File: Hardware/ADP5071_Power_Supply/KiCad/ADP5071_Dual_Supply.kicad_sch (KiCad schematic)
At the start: 42 parts, among them J1 MountingPin, J2 Screw_Terminal_01x02, J3 Conn_01x03_Pin, J4 MountingPin, J5 MountingPin, J6 MountingPin, U1 ADP5071AREZ

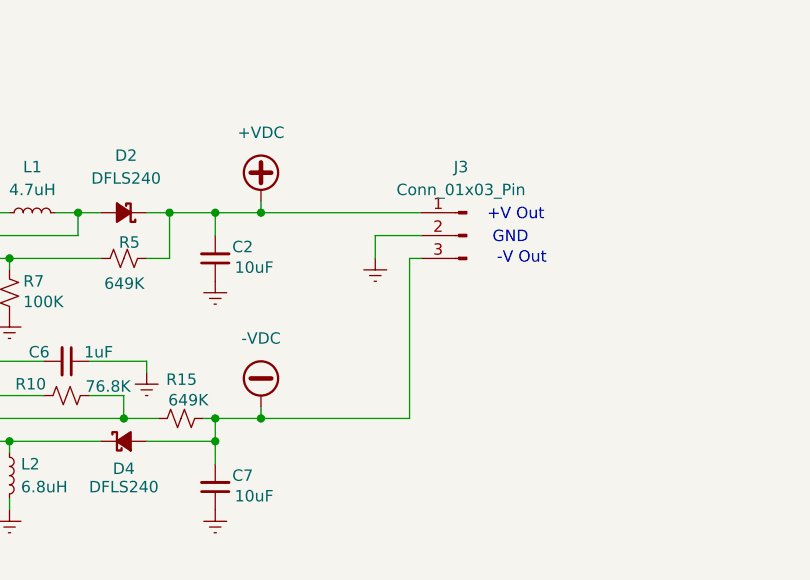
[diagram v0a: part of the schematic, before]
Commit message: added connector for dual board power delivery
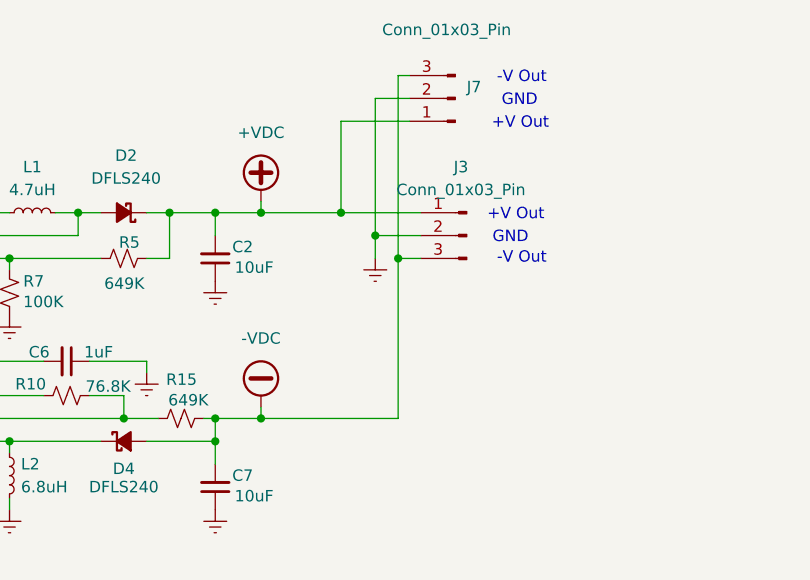
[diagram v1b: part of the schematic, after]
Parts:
- added J7: Conn_01x03_Pin, Connector_PinHeader_2.54mm:PinHeader_1x03_P2.54mm_Horizontal, symbol Connector:Conn_01x03_Pin
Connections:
- net +VDC: now also J7.1 (Pin_1)
- net -VDC: now also J7.3 (Pin_3)
- net GNDREF: now also J7.2 (Pin_2)
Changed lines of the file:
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@@
 		)
 	)
+	(text "-V Out"
+		(exclude_from_sim no)
+		(at 222.25 65.786 0)
+		(effects
+			(font
+				(size 1.27 1.27)
+			)
+			(justify right bottom)
+		)
+	)
 	(text "+V Out"
 		(exclude_from_sim no)
@@
 		)
 	)
+	(text "GND"
+		(exclude_from_sim no)
+		(at 221.234 68.326 0)
+		(effects
+			(font
+				(size 1.27 1.27)
+			)
+			(justify right bottom)
+		)
+	)
+	(text "+V Out"
+		(exclude_from_sim no)
+		(at 222.504 70.866 0)
+		(effects
+			(font
+				(size 1.27 1.27)
+			)
+			(justify right bottom)
+		)
+	)
 	(junction
 		(at 160.02 100.33)
@@
 	)
 	(junction
+		(at 205.74 85.09)
+		(diameter 0)
+		(color 0 0 0 0)
+	)
+	(junction
 		(at 99.06 90.17)
 		(diameter 0)
@@
 	)
 	(junction
+		(at 203.2 82.55)
+		(diameter 0)
+		(color 0 0 0 0)
+	)
+	(junction
 		(at 105.41 133.35)
 		(diameter 0)
@@
 	)
 	(junction
+		(at 199.39 80.01)
+		(diameter 0)
+		(color 0 0 0 0)
+	)
+	(junction
 		(at 127 85.09)
 		(diameter 0)
@@
 	(wire
 		(pts
+			(xy 205.74 85.09) (xy 208.28 85.09)
+		)
+		(stroke
+			(width 0)
+			(type default)
+		)
+	)
+	(wire
+		(pts
 			(xy 80.01 76.2) (xy 80.01 85.09)
 		)
@@
 	(wire
 		(pts
-			(xy 190.5 80.01) (xy 208.28 80.01)
+			(xy 190.5 80.01) (xy 199.39 80.01)
 		)
 		(stroke
@@
 	(wire
 		(pts
+			(xy 207.01 69.85) (xy 199.39 69.85)
+		)
+		(stroke
+			(width 0)
+			(type default)
+		)
+	)
+	(wire
+		(pts
 			(xy 114.3 105.41) (xy 114.3 102.87)
 		)
@@
 	(wire
 		(pts
+			(xy 199.39 80.01) (xy 208.28 80.01)
+		)
+		(stroke
+			(width 0)
+			(type default)
+		)
+	)
+	(wire
+		(pts
 			(xy 78.74 95.25) (xy 78.74 97.79)
 		)
@@
 	(wire
 		(pts
+			(xy 203.2 67.31) (xy 203.2 82.55)
+		)
+		(stroke
+			(width 0)
+			(type default)
+		)
+	)
+	(wire
+		(pts
 			(xy 58.42 69.85) (xy 58.42 76.2)
 		)
@@
 	(wire
 		(pts
+			(xy 205.74 64.77) (xy 205.74 85.09)
+		)
+		(stroke
+			(width 0)
+			(type default)
+		)
+	)
+	(wire
+		(pts
 			(xy 171.45 100.33) (xy 175.26 100.33)
 		)
@@
 	(wire
 		(pts
-			(xy 190.5 102.87) (xy 207.01 102.87)
+			(xy 190.5 102.87) (xy 205.74 102.87)
 		)
 		(stroke
@@
 	(wire
 		(pts
-			(xy 207.01 102.87) (xy 207.01 85.09)
+			(xy 205.74 102.87) (xy 205.74 85.09)
 		)
 		(stroke
@@
 	(wire
 		(pts
+			(xy 199.39 69.85) (xy 199.39 80.01)
+		)
+		(stroke
+			(width 0)
+			(type default)
+		)
+	)
+	(wire
+		(pts
 			(xy 184.15 102.87) (xy 185.42 102.87)
 		)
@@
 	(wire
 		(pts
+			(xy 207.01 64.77) (xy 205.74 64.77)
+		)
+		(stroke
+			(width 0)
+			(type default)
+		)
+	)
+	(wire
+		(pts
 			(xy 127 82.55) (xy 127 85.09)
 		)
@@
 	(wire
 		(pts
-			(xy 207.01 85.09) (xy 208.28 85.09)
+			(xy 203.2 67.31) (xy 207.01 67.31)
 		)
 		(stroke
@@
 					(unit 1)
 				)
+			)
+		)
+	)
+	(symbol
+		(lib_id "Connector:Conn_01x03_Pin")
+		(at 212.09 67.31 180)
+		(unit 1)
+		(exclude_from_sim no)
+		(in_bom yes)
+		(on_board yes)
+		(dnp no)
+		(property "Reference" "J7"
+			(at 213.36 66.0399 0)
+			(effects
+				(font
+					(size 1.27 1.27)
+				)
+				(justify right)
+			)
+		)
+		(property "Value" "Conn_01x03_Pin"
+			(at 203.962 59.69 0)
+			(effects
+				(font
+					(size 1.27 1.27)
+				)
+				(justify right)
+			)
+		)
+		(property "Footprint" "Connector_PinHeader_2.54mm:PinHeader_1x03_P2.54mm_Horizontal"
+			(at 212.09 67.31 0)
+			(effects
+				(font
+					(size 1.27 1.27)
+				)
+				(hide yes)
+			)
+		)
+		(property "Datasheet" "~"
+			(at 212.09 67.31 0)
+			(effects
+				(font
+					(size 1.27 1.27)
+				)
+				(hide yes)
+			)
+		)
+		(property "Description" "Generic connector, single row, 01x03, script generated"
+			(at 212.09 67.31 0)
+			(effects
+				(font
+					(size 1.27 1.27)
+				)
+				(hide yes)
+			)
+		)
+		(pin "1"
+		)
+		(pin "3"
+		)
+		(pin "2"
+		)
+		(instances
+			(project ""
+				(path "/359c8d50-ab92-45cb-a3ea-95ee484a708c"
+					(reference "J7")
+					(unit 1)
+				)
